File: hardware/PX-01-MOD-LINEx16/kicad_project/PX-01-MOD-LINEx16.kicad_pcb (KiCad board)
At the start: 2 copper layers, 141.2 x 30.9 mm, 55 parts, among them J8 Conn_01x07_Socket, J9 Conn_01x08

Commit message: Añade Revisión y Modelos 3D
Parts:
- AUX_FLEX1: footprint Connector_FFC-FPC:TE_0-1734839-8_1x08-1MP_P0.5mm_Horizontal -> custom_footprints:FPC0.5-8P
- FLEX_MORRO1: renamed from FLEX; footprint Connector_FFC-FPC:TE_0-1734839-8_1x08-1MP_P0.5mm_Horizontal -> custom_footprints:FPC0.5-8P
- moved J9 16.0 mm to (146.7, 102.0), turned to -90 degrees
- moved C3 15.1 mm to (161.5, 106.7), turned to 0 degrees
- moved C1 15.1 mm to (147.0, 106.7), turned to 180 degrees
- moved C4 14.5 mm to (161.5, 105.0), turned to 0 degrees
- moved C2 14.5 mm to (147.0, 105.0), turned to 180 degrees
- moved AUX_FLEX1 2.36 mm to (154.2, 105.7), turned to 180 degrees
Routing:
- net /AUX_3.3_M: track 31.3 -> 31.7 mm, vias 7 -> 8
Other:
- board text added: "JLCJLCJLCJLC"
- board text added: "Rev. 1.0"
- board text removed: "3.3"
- board text removed: "WayWayWay"

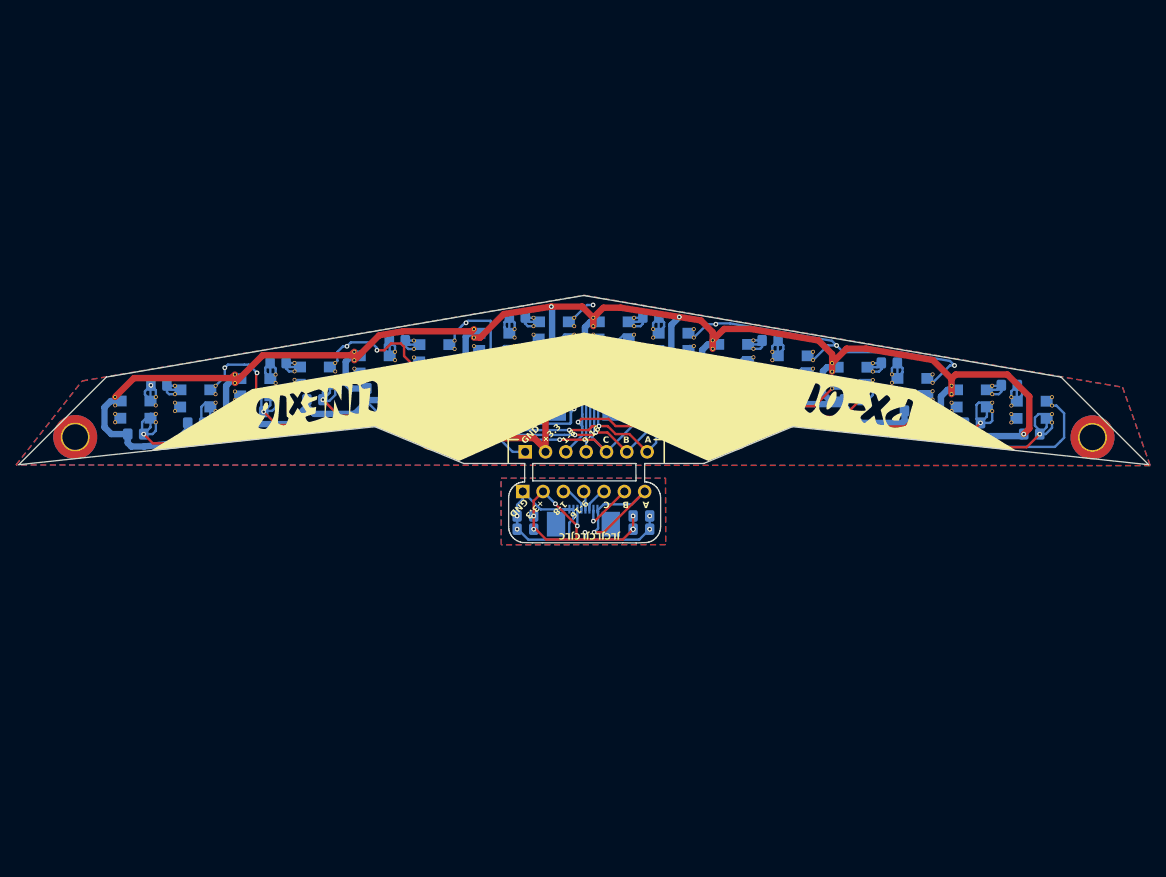
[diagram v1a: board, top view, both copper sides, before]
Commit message: Actualiza Silkscreen para PCB en negro y añade referencias LCSC
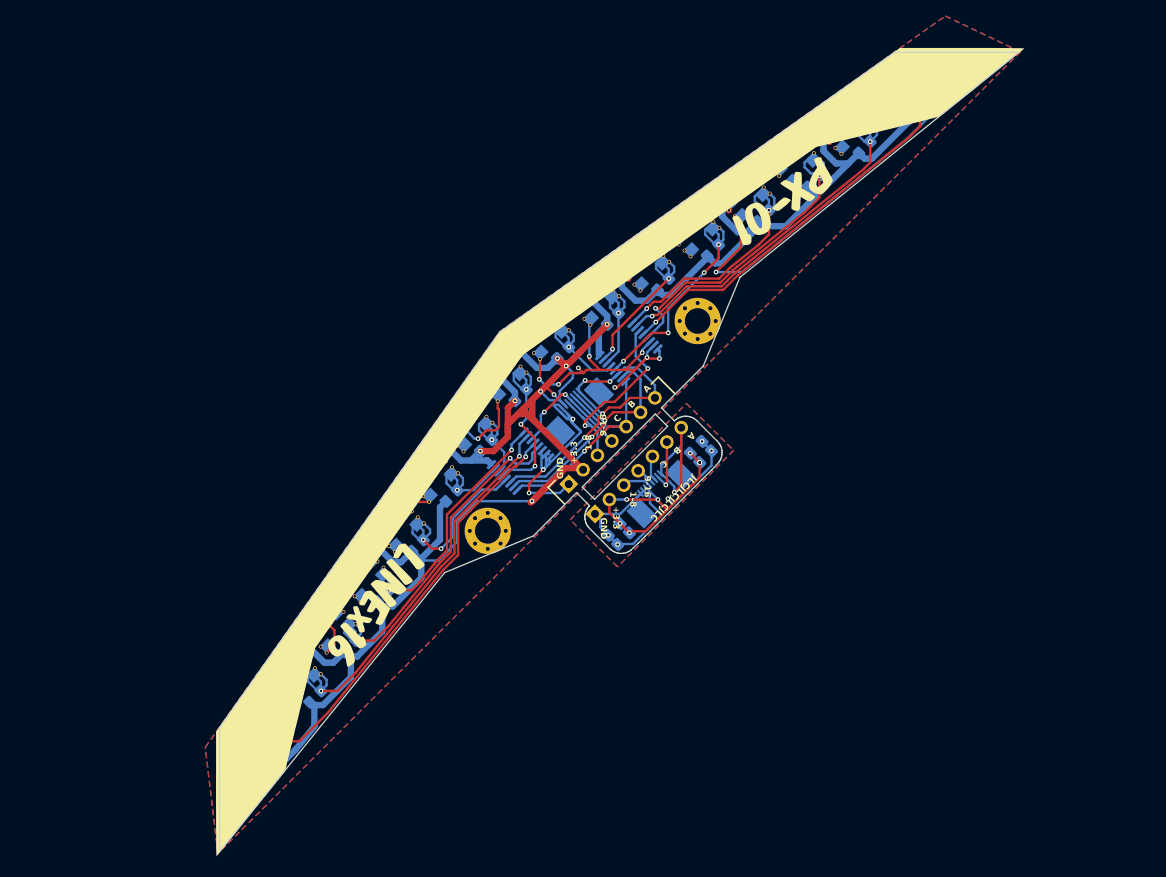
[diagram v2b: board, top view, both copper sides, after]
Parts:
- removed ?: , LOGO
- added G***: LOGO, LOGO, F.Cu at (143.8, 82.0)
- MUX1, MUX2: footprint Package_SO:TSSOP-16_4.4x5mm_P0.65mm -> custom_footprints:MUX_CD4051B
- moved REF** 48.9 mm to (111.3, 139.5), turned to 45 degrees
- moved REF** 48.5 mm to (201.3, 49.6), turned to 45 degrees
- moved R2 43.1 mm to (116.4, 133.9), turned to -135 degrees
- moved S1 43.1 mm to (114.2, 131.7), turned to 45 degrees
- moved R24 42.7 mm to (195.6, 54.7), turned to -135 degrees
- moved S16 42.7 mm to (193.5, 52.6), turned to 45 degrees
- moved R1 41.0 mm to (114.2, 127.5), turned to 45 degrees
- moved R22 40.6 mm to (189.3, 52.4), turned to 45 degrees
- moved S2 37.4 mm to (118.5, 125.5), turned to 45 degrees
- moved R3 37.3 mm to (120.7, 127.6), turned to -135 degrees
- moved R23 37.0 mm to (189.4, 58.9), turned to -135 degrees
- moved S15 37.0 mm to (187.2, 56.8), turned to 45 degrees
- moved S3 31.7 mm to (122.8, 119.2), turned to 45 degrees
- moved R5 31.6 mm to (125.0, 121.3), turned to -135 degrees
- moved S14 31.3 mm to (180.9, 61.1), turned to 45 degrees
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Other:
- board size 141.2 x 30.9 mm -> 99.9 x 99.9 mm

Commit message: Añade gerbers y actualiza flex a 7P. Cambia la referencia de algunos componentes
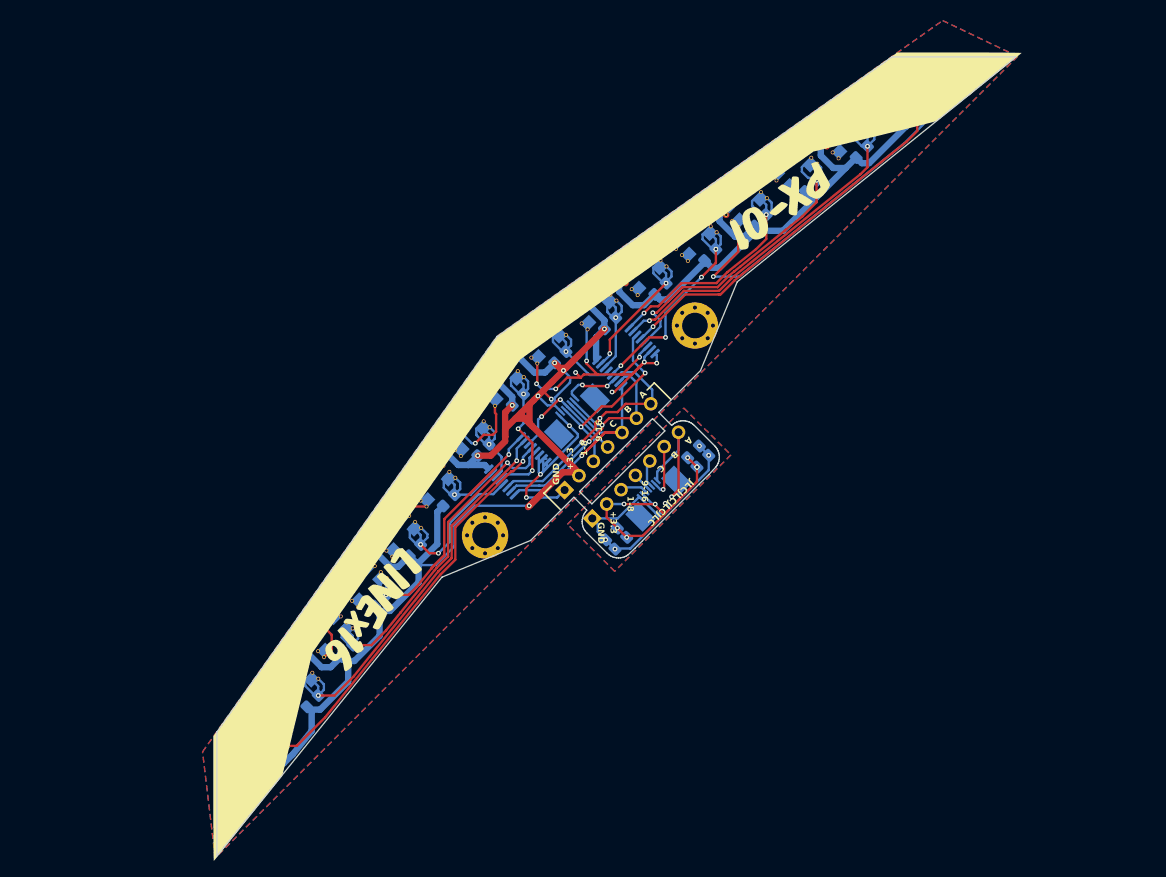
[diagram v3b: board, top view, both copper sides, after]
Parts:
- AUX_FLEX1, FLEX_MORRO1: value Conn_01x08 -> Conn_01x07; footprint custom_footprints:FPC0.5-8P -> Connector_FFC-FPC:TE_0-1734839-7_1x07-1MP_P0.5mm_Horizontal
- moved J8 0.91 mm to (151.9, 101.8)
- moved R20 0.66 mm to (176.4, 68.1)
- moved R11 0.66 mm to (141.7, 96.8)
- moved C3 0.66 mm to (169.2, 98.2)
- moved R16 0.66 mm to (163.9, 70.1)
- moved R9 0.66 mm to (137.4, 103.1)
- moved R13 0.66 mm to (151.3, 78.6)
- moved R14 0.66 mm to (151.4, 85.2)
- moved S11 0.66 mm to (161.7, 74.5)
- moved R22 0.66 mm to (189.0, 52.9)
- moved REF** 0.66 mm to (142.0, 107.4)
- moved R15 0.66 mm to (157.6, 80.9)
- moved S3 0.66 mm to (122.5, 119.7)
- moved C1 0.66 mm to (158.9, 108.4)
- moved S2 0.66 mm to (118.2, 126.0)
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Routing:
- net /GND_M: track 217.9 -> 208.7 mm
- net /CH_C: track 30.6 -> 36.7 mm
- net /CH_A: track 40.8 -> 37.8 mm
- net /AUX_CH_A: track 18.3 -> 15.6 mm
- net /OUT2: track 27.0 -> 24.5 mm
- net /3.3_M: track 405.7 -> 404.0 mm
- net /AUX_CH_C: track 3.31 -> 3.81 mm
